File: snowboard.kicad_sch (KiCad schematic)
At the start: 30 parts, among them J1 Micro USB Port, Q1 S8050, Q2 S8050, SW1 RESET, SW2 BOOT, U1 ESP32-WROVER-E-N4R8, U2 CP2102N-A02-GQFN28R, U3 SPX3819M5-L-3-3, U4 MCP73831-2-OT

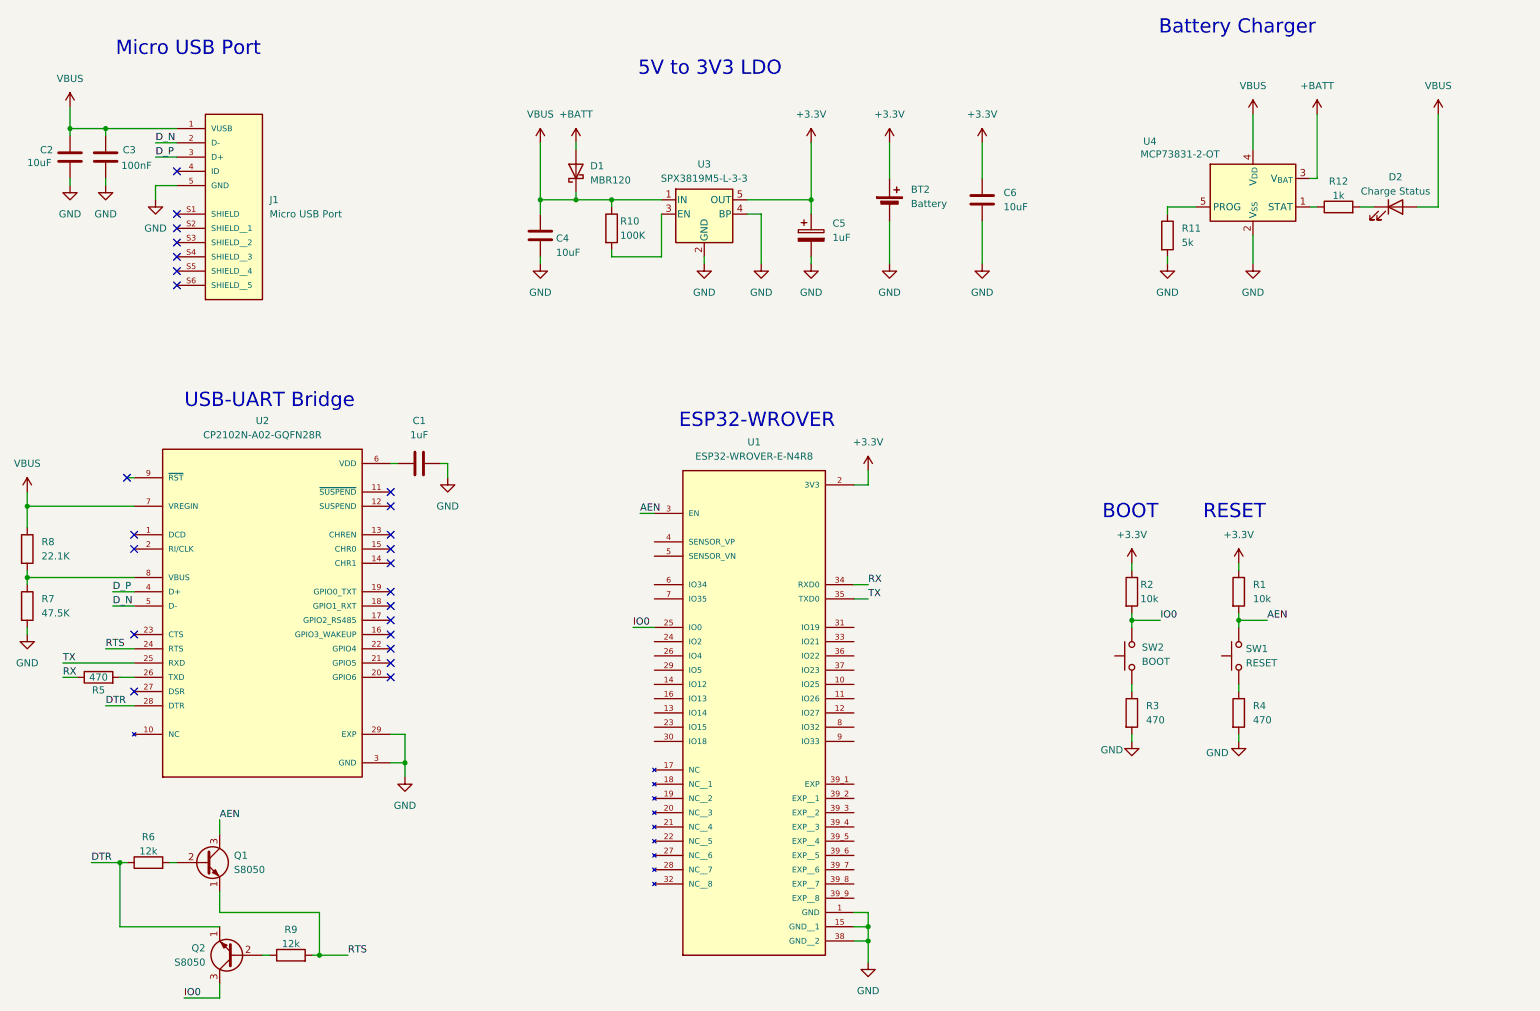
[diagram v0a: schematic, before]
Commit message: Update battery connector
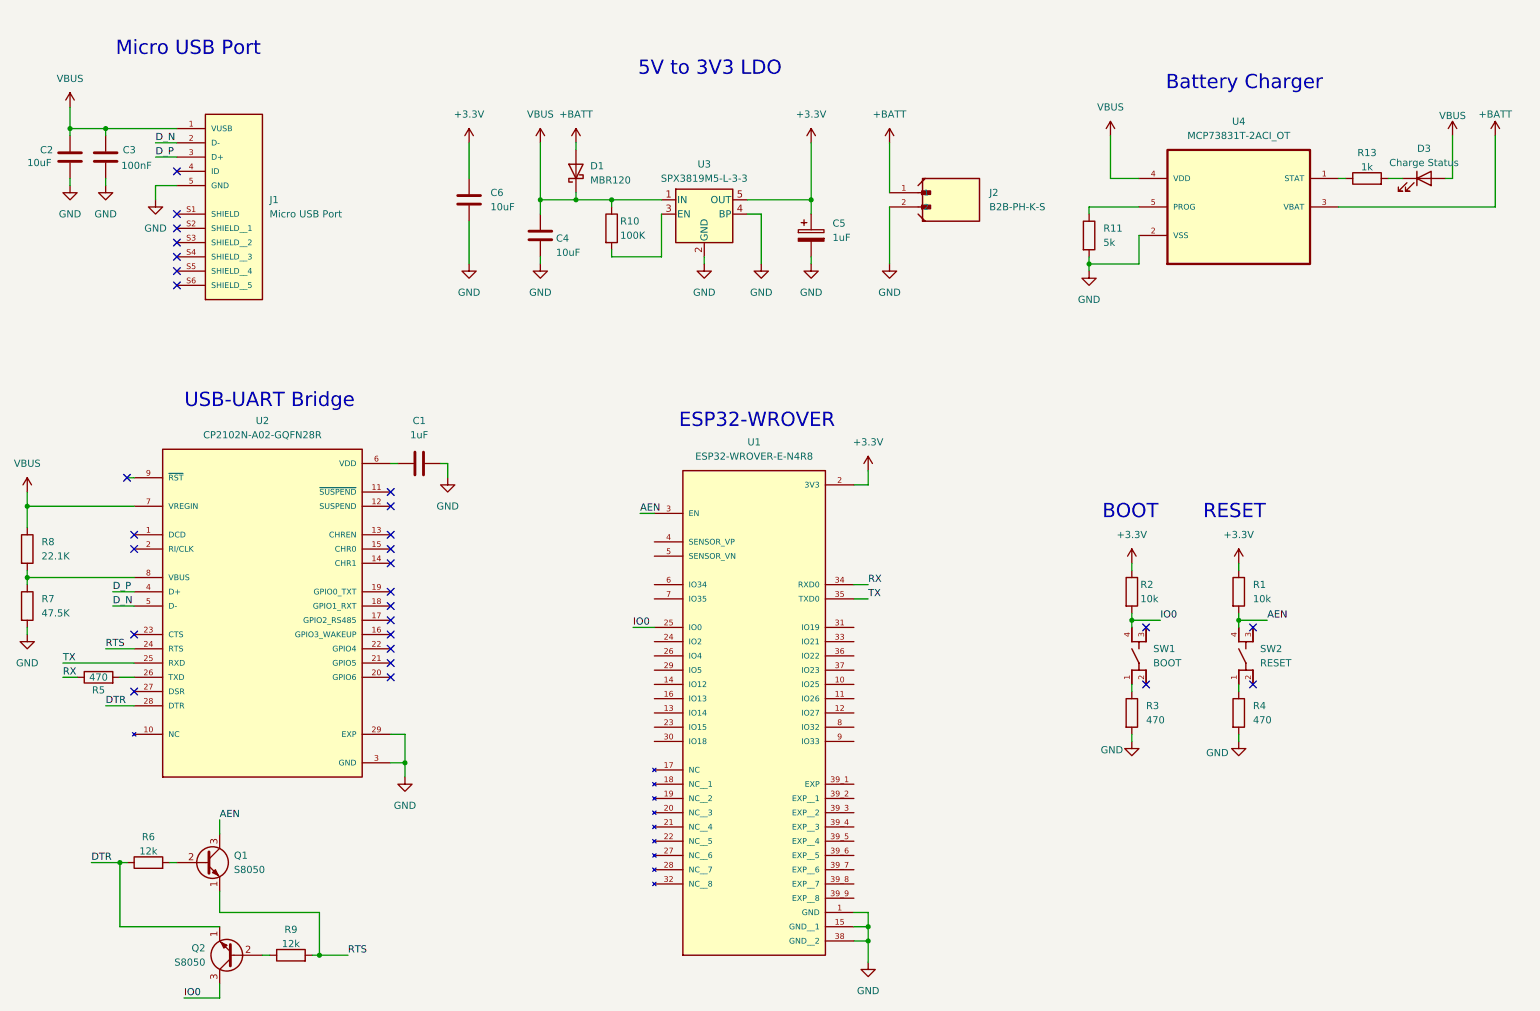
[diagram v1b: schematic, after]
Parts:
- removed BT2: Battery, symbol Device:Battery_Cell
- removed D2: Charge Status, symbol Device:LED
- removed R12: 1k, symbol Device:R
- removed SW1: RESET, symbol Switch:SW_Push
- removed SW2: BOOT, symbol Switch:SW_Push
- removed U4: MCP73831-2-OT, Package_TO_SOT_SMD:SOT-23-5, symbol Battery_Management:MCP73831-2-OT
- added D3: Charge Status, symbol Device:LED
- added J2: B2B-PH-K-S, B2B-PH-K-S:JST_B2B-PH-K-S, symbol Battery_Conn:B2B-PH-K-S
- added R13: 1k, symbol Device:R
- added SW1: BOOT, PTS810_SJM_250_SMTR_LFS:SW_PTS810_SJM_250_SMTR_LFS, symbol PTS810_Btn:PTS810_SJM_250_SMTR_LFS
- added SW2: RESET, PTS810_SJM_250_SMTR_LFS:SW_PTS810_SJM_250_SMTR_LFS, symbol PTS810_Btn:PTS810_SJM_250_SMTR_LFS
- added U4: MCP73831T-2ACI_OT, MCP73831T-2ACI_OT:SOT95P280X145-5N, symbol MCP73831-2ACI_OT:MCP73831T-2ACI_OT
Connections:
- net +BATT: now also J2.1, U4.3 (VBAT)
- net AEN: now also SW2.4
- net GND: now also J2.2, U4.2 (VSS)
- net IO0: now also SW1.4
- net VBUS: now also D3.2 (A), U4.4 (VDD)
- net at R4.1: now also SW2.1
- net at R11.1: now also U4.5 (PROG)
- net at R3.1: now also SW1.1
- new net: D3.1 (K), R13.2
- new net: R13.1, U4.1 (STAT)
- no-connect marks 24 -> 28
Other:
- moved on the sheet: C6, R11

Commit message: PCB routing mostly done
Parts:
- added U5: MPU-6050, QFN24_4X4X0P9-0P5_TDK, symbol MPU6050:MPU-6050
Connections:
- no-connect marks 28 -> 54
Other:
- moved on the sheet: R1, R2, R3, R4, SW1, SW2

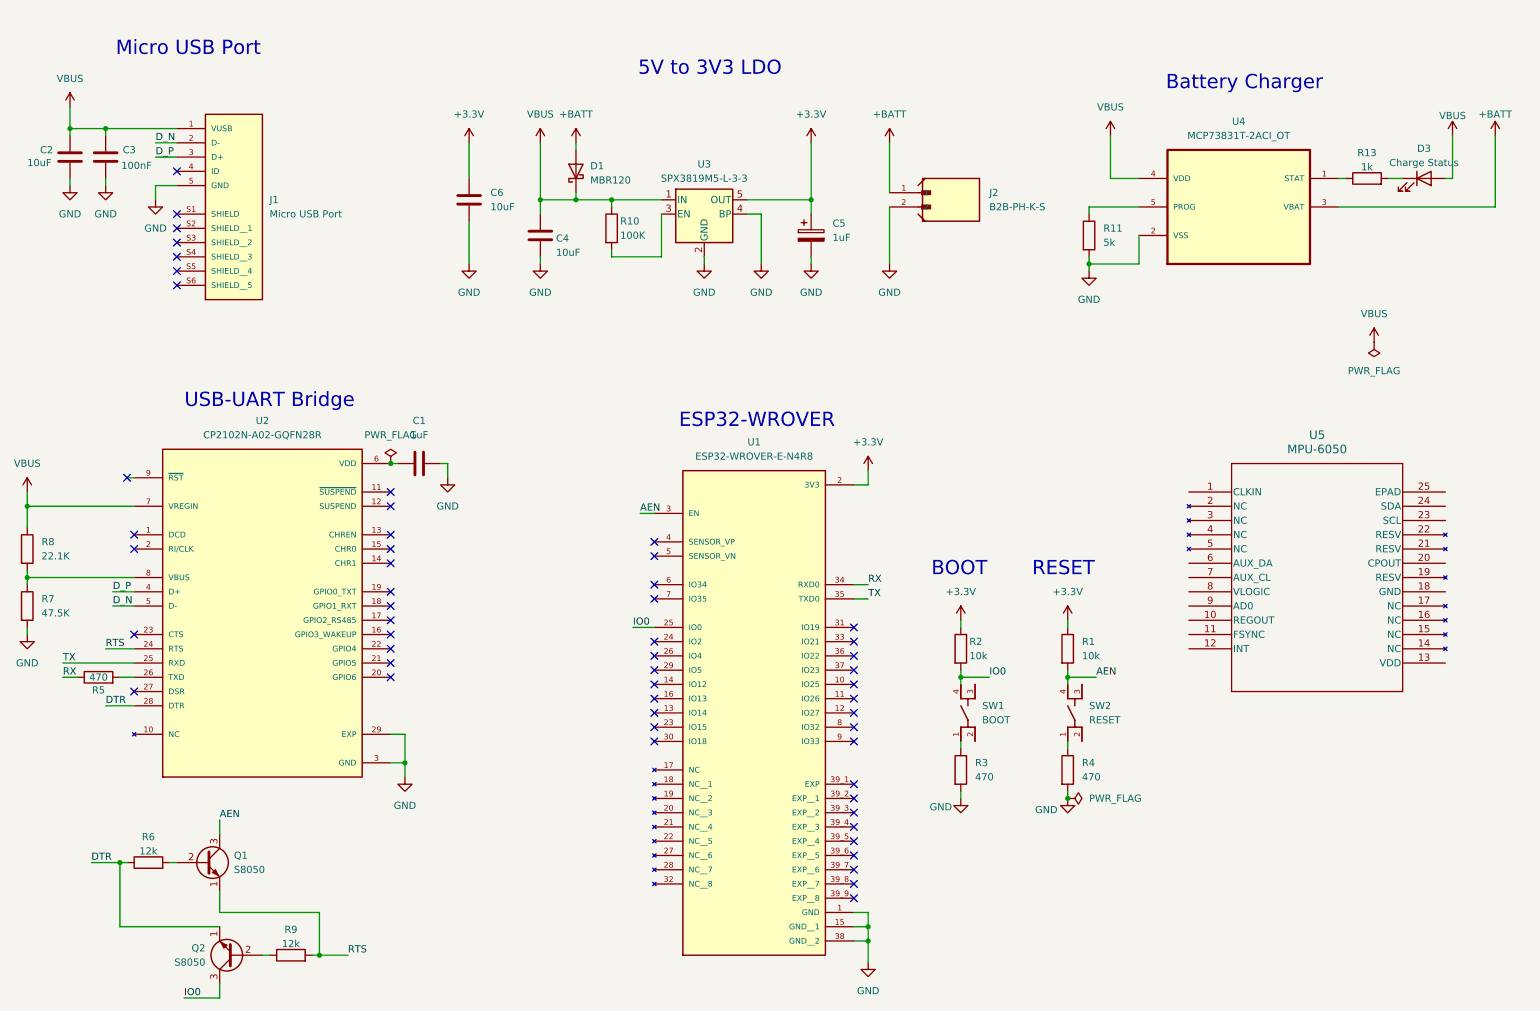
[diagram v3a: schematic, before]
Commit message: Add IMU
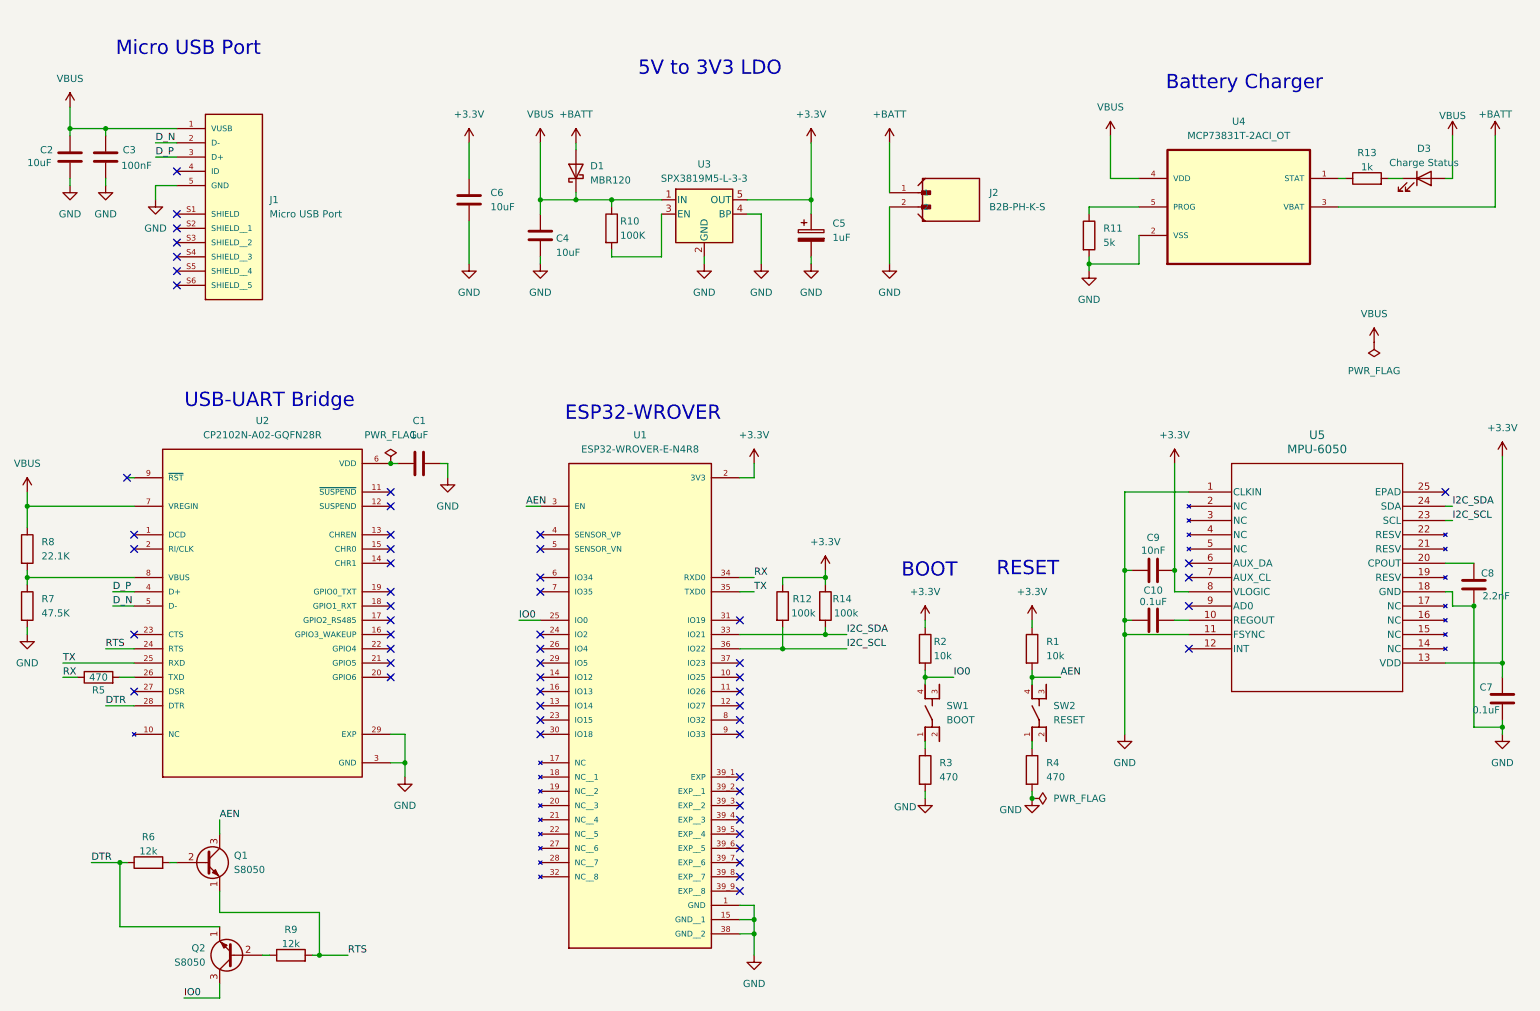
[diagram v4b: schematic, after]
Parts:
- added C10, C7: 0.1uF, symbol Device:C
- added C8: 2.2nF, symbol Device:C
- added C9: 10nF, symbol Device:C
- added R12, R14: 100k, symbol Device:R
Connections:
- net +3.3V: now also U5.13 (VDD), U5.8 (VLOGIC), C7.1, C9.2, R12.1, R14.1
- net GND: now also U5.1 (CLKIN), U5.11 (FSYNC), U5.18 (GND), C10.1, C7.2, C8.2, C9.1
- net at U5.10 (REGOUT): now also C10.2
- net at U5.20 (CPOUT): now also C8.1
- net I2C_SCL: now reaches U5.23 (SCL)
- net I2C_SCL: now also U1.36 (IO22), R12.2
- net I2C_SDA: now reaches U5.24 (SDA)
- net I2C_SDA: now also U1.33 (IO21), R14.2
- no-connect marks 54 -> 57
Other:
- moved on the sheet: R1, R2, R3, R4, SW1, SW2, U1

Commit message: Add test points
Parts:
- added TP1, TP10, TP11, TP12, TP13, TP14, TP15, TP16, TP17, TP18, TP19, TP2, TP20, TP21, TP22, TP23, TP24, TP25, TP3, TP4, TP5, TP6, TP7, TP8, TP9: TestPoint, symbol Connector:TestPoint
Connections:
- net +3.3V: now also TP20.1
- net +BATT: now also TP18.1
- net GND: now also TP19.1, TP21.1, TP23.1
- net I2C_SCL: now also TP16.1
- net I2C_SDA: now also TP17.1
- net RX: now also TP24.1
- net TX: now also TP25.1
- net VBUS: now also TP22.1
- net at U1.10 (IO25): now also TP11.1
- net at U1.11 (IO26): now also TP12.1
- net at U1.12 (IO27): now also TP13.1
- net at U1.13 (IO14): now also TP6.1
- net at U1.14 (IO12): now also TP4.1
- net at U1.16 (IO13): now also TP5.1
- net at U1.23 (IO15): now also TP7.1
- net at U1.24 (IO2): now also TP1.1
- net at U1.26 (IO4): now also TP2.1
- net at U1.29 (IO5): now also TP3.1
- net at U1.30 (IO18): now also TP8.1
- net at U1.31 (IO19): now also TP9.1
- net at U1.37 (IO23): now also TP10.1
- net at U1.8 (IO32): now also TP14.1
- net at U1.9 (IO33): now also TP15.1
- no-connect marks 57 -> 42
